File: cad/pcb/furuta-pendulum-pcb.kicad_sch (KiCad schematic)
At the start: 8 parts, among them J1 Motor_Encoder, J2 AMT103-V, J3 Pololu TB9051FTG Driver, SW1 SW_SPDT_312, SW2 SW_SPDT_312, SW3 SW_SPDT_312, U1 Teesny 3.6, U2 LM78L05_TO92

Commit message: update pcb files
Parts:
- added D1: LD271, LED_THT:LED_D5.0mm_IRGrey, symbol LED:LD271
- added J4: CT3151SP-0 (BLK), Connector:CalTest_CT3151, symbol Connector:Screw_Terminal_01x01
- added J5: CT3151SP-2 (RED), Connector:CalTest_CT3151, symbol Connector:Screw_Terminal_01x01
- added J6, J7: Conn_01x02, Connector_PinHeader_2.54mm:PinHeader_1x02_P2.54mm_Vertical, symbol Connector_Generic:Conn_01x02
- J1: value Motor_Encoder -> Pololu Motor+Encoder; footprint (none) -> Connector_PinHeader_2.54mm:PinHeader_1x06_P2.54mm_Vertical; symbol Teensy:Motor_Encoder -> Teensy:Pololu Motor+Encoder
- J2: footprint (none) -> Connector_PinHeader_2.54mm:PinHeader_1x04_P2.54mm_Vertical
- J3: footprint (none) -> Library:Pololu TB9051FTG motor driver
- SW1, SW2, SW3: footprint (none) -> Library:Flat Toggle Switch
- U1: footprint Teensy 3.6 -> Library:Teensy 3.6
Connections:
- net +5V: now also J1.4 (Enc_Vcc), J2.1 (5V)
- net GND: now also J1.3 (Enc_GND), J2.2 (GND), J3.13 (GND), SW1.3 (A), SW2.3 (A), SW3.3 (A), U1.1 (GND), U1.34 (GND), D1.1 (K), J4.1 (Pin_1), J6.2 (Pin_2), J7.2 (Pin_2)
- net PWM1: now also U1.5 (3); no longer U1.28 (36)
- net PWM2: now also U1.6 (4); no longer U1.27 (35)
- net VM: now reaches U2.3 (VI)
- net VM: now also J3.1 (VM)
- net at J1.1 (Motor_PWR): now also J3.12 (OUT2)
- net at J1.2 (Motor_PWR): now also J3.11 (OUT1)
- net ENC1_A: now reaches J1.5 (Enc_A)
- net ENC1_A: now also U1.11 (9)
- net ENC1_B: now reaches J1.6 (Enc_B)
- net ENC1_B: now also U1.12 (10)
- net +12V: now reaches J3.14 (VIN)
- net +12V: now also J5.1 (Pin_1)
- net OCM: now reaches J3.9 (OCM)
- net OCM: now also U1.4 (2)
- net SW3: now reaches SW3.1 (B)
- net SW3: now also U1.35 (13)
- net SW2: now reaches SW2.1 (B)
- net SW2: now also U1.30 (38)
- net ENC2_B: now reaches U1.21 (29)
- net ENC2_B: now also J2.3 (B)
- net ENC2_A: now reaches U1.22 (30)
- net ENC2_A: now also J2.4 (A)
- net SW1: now reaches U1.26 (34)
- net SW1: now also SW1.1 (B)
- net TIMER_1: now reaches U1.38 (16)
- net TIMER_1: now also J6.1 (Pin_1)
- net TIMER_2: now reaches U1.42 (20)
- net TIMER_2: now also J7.1 (Pin_1)
- net at U1.45 (23): now also D1.2 (A)
- no-connect marks 3 -> 37
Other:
- moved on the sheet: J1, J2, SW1, SW2, SW3, U1, U2

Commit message: add current sensor breakout board
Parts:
- added U3: ~, Library:Pololu ACS724 Current Sensor, symbol Teensy:Pololu_ACS724_Current_Sensor
- J2: footprint Connector_PinHeader_2.54mm:PinHeader_1x04_P2.54mm_Vertical -> Connector_PinSocket_2.54mm:PinSocket_1x04_P2.54mm_Vertical
- J4: value CT3151SP-0 (BLK) -> Screw_Terminal_01x01
- J5: value CT3151SP-2 (RED) -> Screw_Terminal_01x01
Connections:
- net +5V: now also U3.2 (VCC)
- net GND: now also U3.1 (GND)
- net at J1.1 (Motor_PWR): now also U3.5 (IP+); no longer J3.12 (OUT2)
- net ISENS: now reaches U1.24 (32)
- net ISENS: now also U3.3 (OUT)
- new net: J3.12 (OUT2), U3.4 (IP-)
- no-connect marks 37 -> 36
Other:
- moved on the sheet: J1

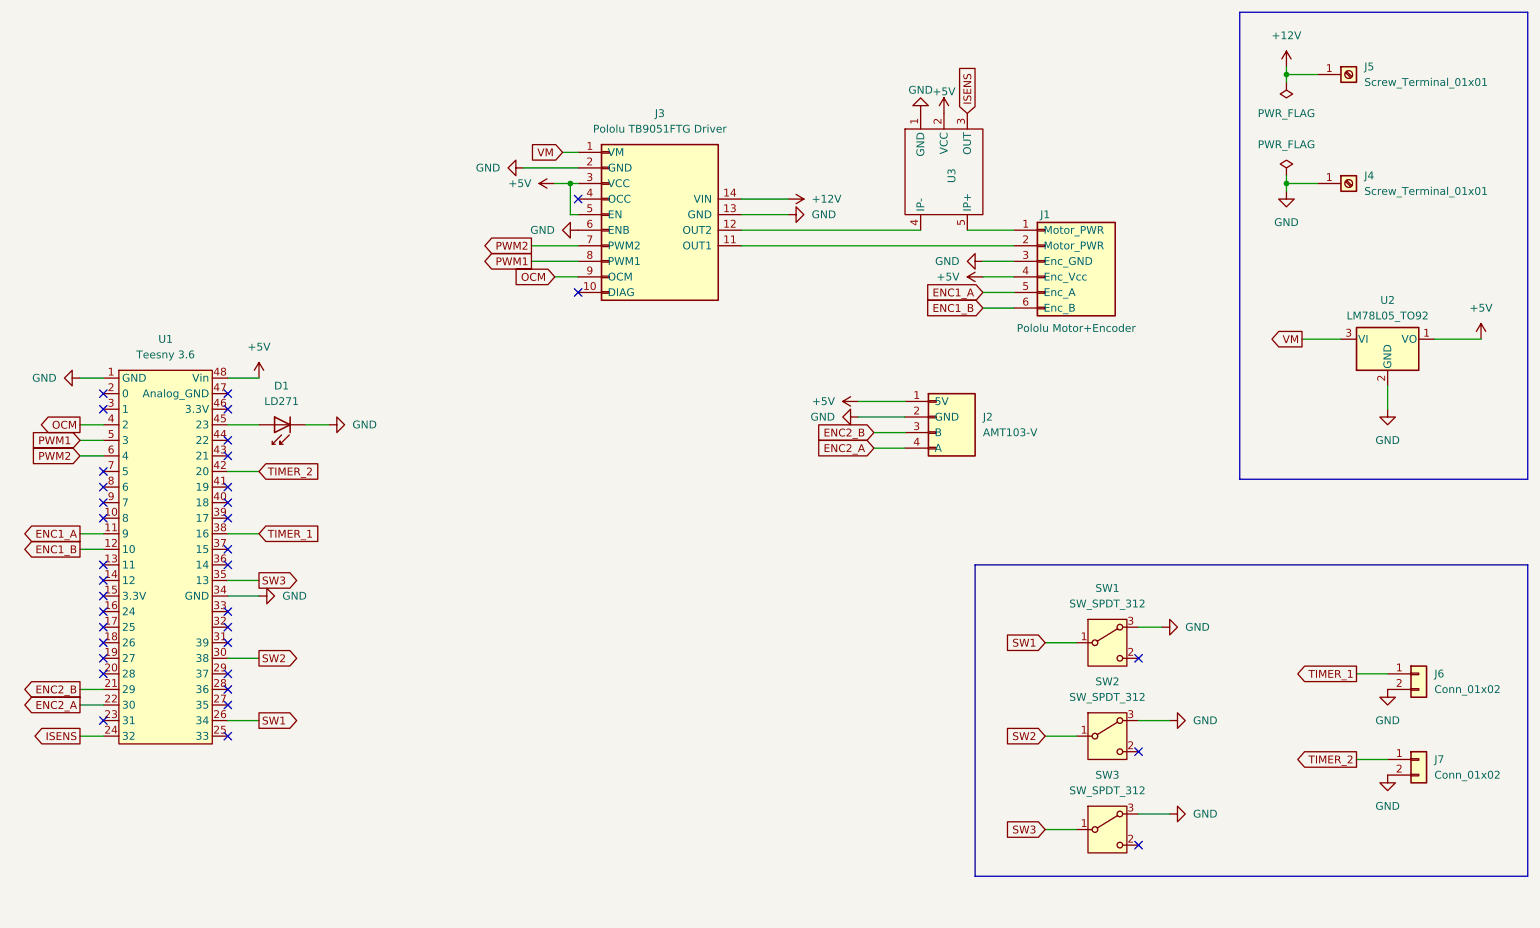
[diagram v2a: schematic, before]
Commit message: create pcb traces, add mounting holes
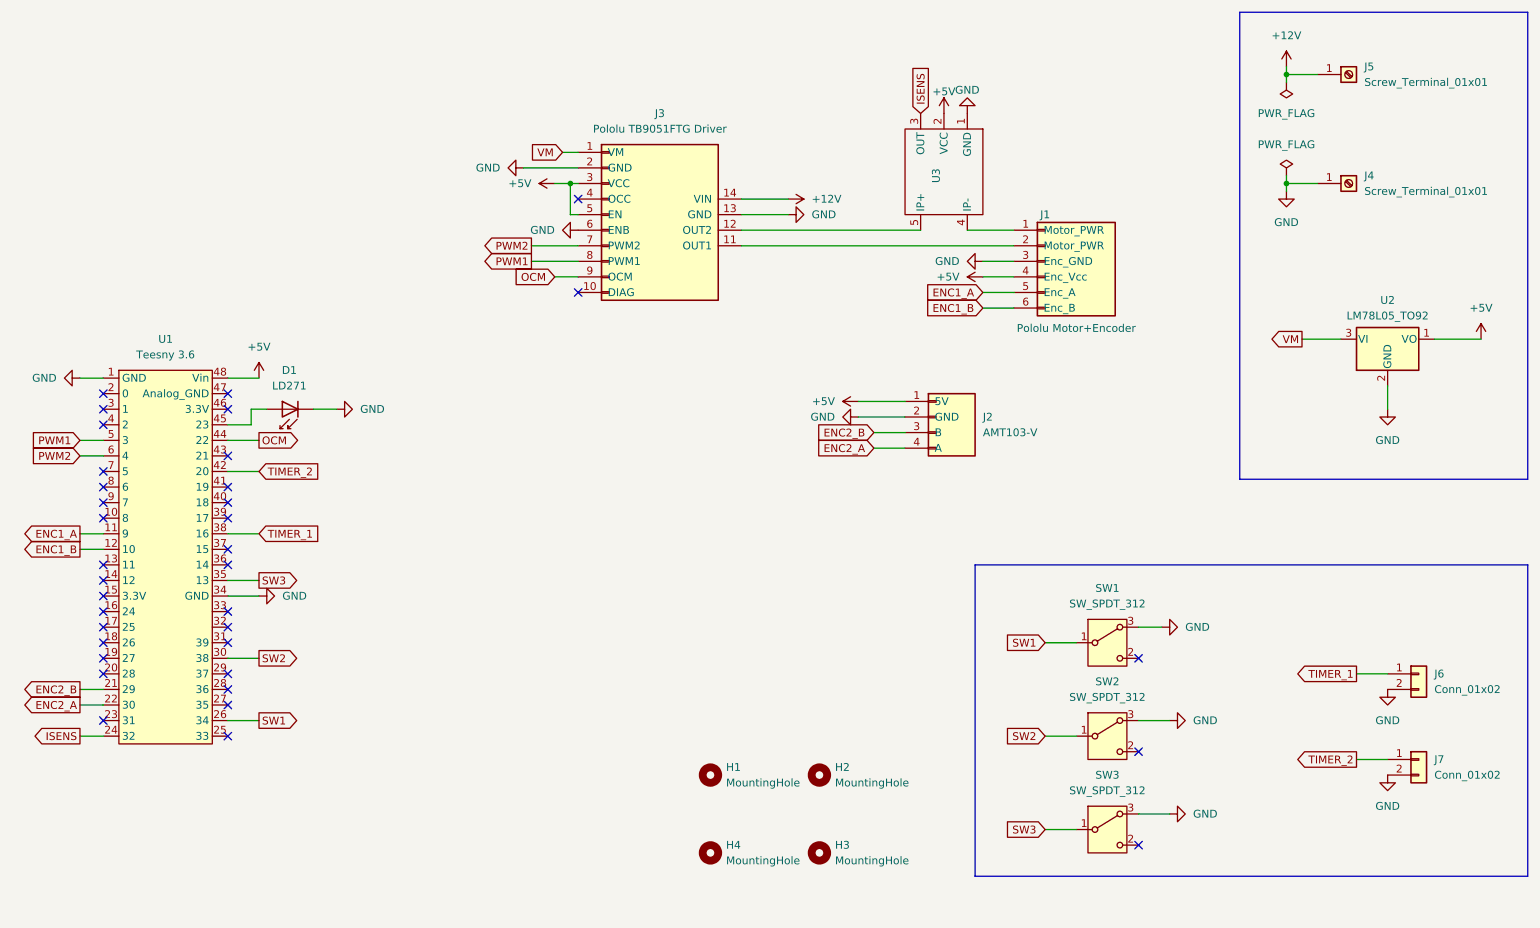
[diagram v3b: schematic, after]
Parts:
- added H1, H2, H3, H4: MountingHole, MountingHole:MountingHole_2.2mm_M2, symbol Mechanical:MountingHole
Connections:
- net OCM: now also U1.44 (22); no longer U1.4 (2)
- net at J1.1 (Motor_PWR): now also U3.4 (IP-); no longer U3.5 (IP+)
- net at J3.12 (OUT2): now also U3.5 (IP+); no longer U3.4 (IP-)
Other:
- moved on the sheet: D1, U3

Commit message: heatsink sizing math, small schematic renames and moves
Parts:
- U3: value ~ -> ACS724LLCTR-2P5AB Current Sensor Carrier -2.5A to +2.5 A
- renumbered J6 to TMR1, J7 to TMR2
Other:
- moved on the sheet: D1, H1, H2, H3, H4, TMR1, TMR2, U1
